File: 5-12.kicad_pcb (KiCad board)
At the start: 2 copper layers, 266.7 x 95.2 mm, 136 parts, among them SW1 SW_Push, U1 ATmega32U4-AU, Y1 16MHz

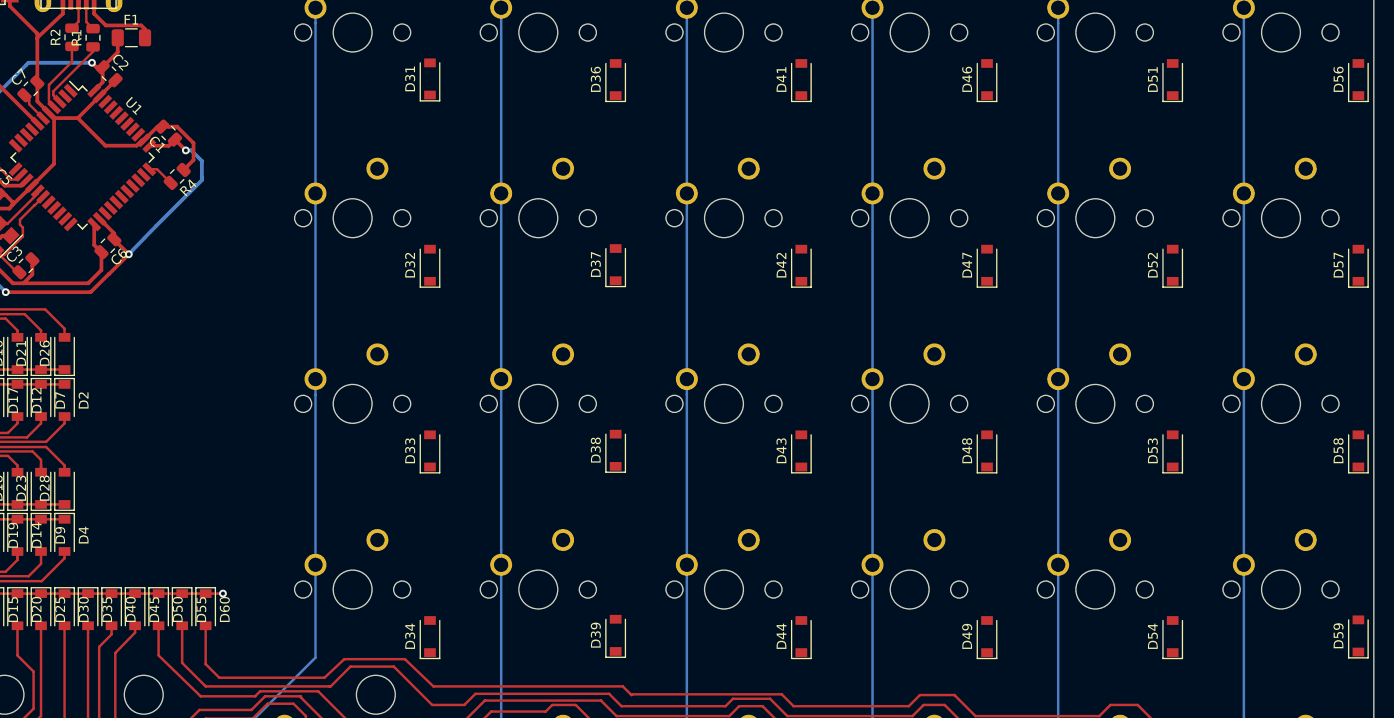
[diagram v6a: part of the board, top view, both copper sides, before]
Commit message: Positioned remainder of diode banks
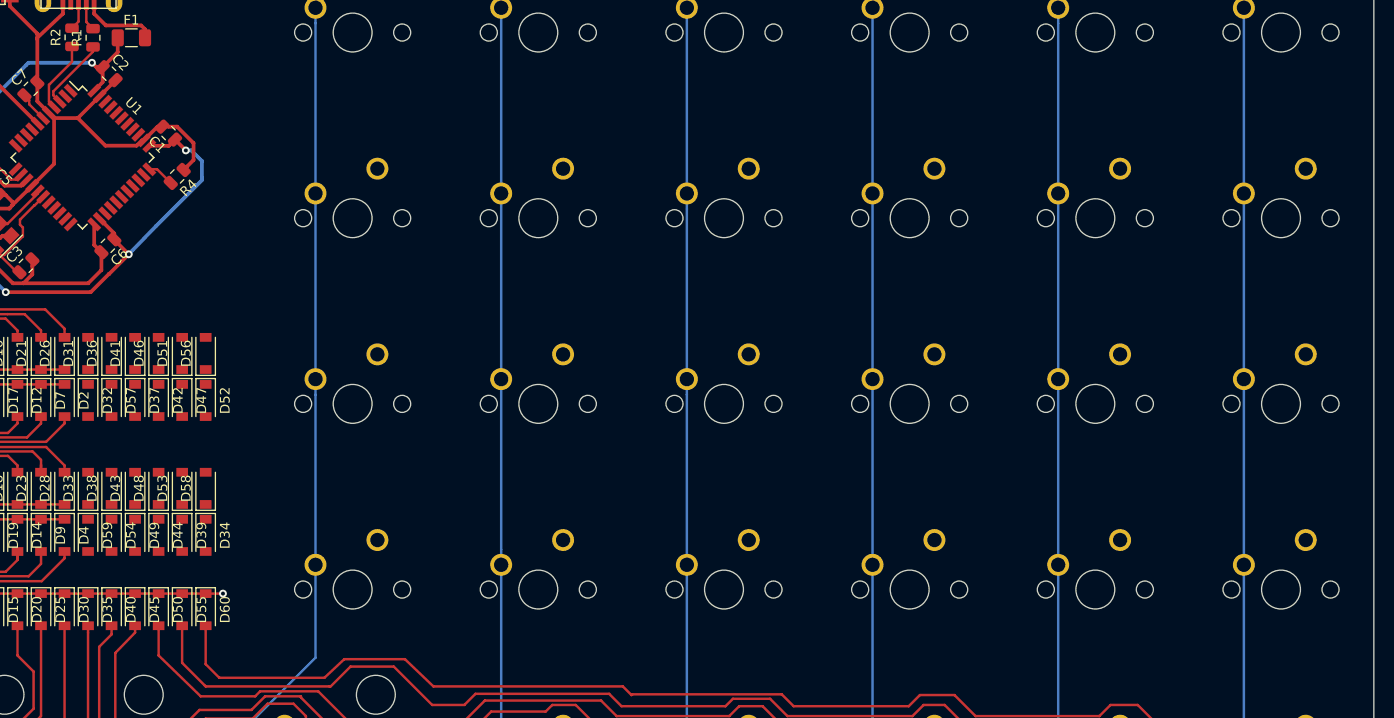
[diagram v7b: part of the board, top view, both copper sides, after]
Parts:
- moved D59 130.7 mm to (146.7, 130.2), turned to 270 degrees
- moved D57 128.7 mm to (149.1, 116.3), turned to 270 degrees
- moved D56 121.6 mm to (158.8, 111.5)
- moved D58 118.3 mm to (158.8, 125.3)
- moved D54 109.4 mm to (149.1, 130.2), turned to 270 degrees
- moved D51 105.4 mm to (156.3, 111.5)
- moved D53 101.7 mm to (156.3, 125.3)
- moved D52 100.2 mm to (158.8, 116.3), turned to 270 degrees
- moved D46 89.5 mm to (153.9, 111.5)
- moved D49 88.0 mm to (151.5, 130.2), turned to 270 degrees
- moved D48 85.1 mm to (153.9, 125.3)
- moved D47 83.7 mm to (156.3, 116.3), turned to 270 degrees
- moved D41 73.9 mm to (151.5, 111.5)
- moved D43 68.5 mm to (151.5, 125.3)
- moved D42 67.4 mm to (153.9, 116.3), turned to 270 degrees
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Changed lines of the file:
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@@
   )
   (module Diode_SMD:D_SOD-123 (layer F.Cu)
-    (at 277.01875 140.49375 90)
+    (at 146.685 130.174 270)
     (descr SOD-123)
     (tags SOD-123)
@@
       (effects (font (size 1 1) (thickness 0.15)))
     )
-    (pad 2 smd rect (at 1.65 0 90) (size 0.9 1.2) (layers F.Cu F.Paste F.Mask)
+    (pad 2 smd rect (at 1.65 0 270) (size 0.9 1.2) (layers F.Cu F.Paste F.Mask)
       (net 69 "Net-(D59-Pad2)"))
-    (pad 1 smd rect (at -1.65 0 90) (size 0.9 1.2) (layers F.Cu F.Paste F.Mask)
+    (pad 1 smd rect (at -1.65 0 270) (size 0.9 1.2) (layers F.Cu F.Paste F.Mask)
       (net 13 Row3))
     (model ${KISYS3DMOD}/Diode_SMD.3dshapes/D_SOD-123.wrl
@@
   )
   (module Diode_SMD:D_SOD-123 (layer F.Cu)
-    (at 277.01875 121.50625 90)
+    (at 158.75 125.35 90)
     (descr SOD-123)
     (tags SOD-123)
@@
   )
   (module Diode_SMD:D_SOD-123 (layer F.Cu)
-    (at 277.01875 102.45625 90)
+    (at 149.098 116.331 270)
     (descr SOD-123)
     (tags SOD-123)
@@
       (effects (font (size 1 1) (thickness 0.15)))
     )
-    (pad 2 smd rect (at 1.65 0 90) (size 0.9 1.2) (layers F.Cu F.Paste F.Mask)
+    (pad 2 smd rect (at 1.65 0 270) (size 0.9 1.2) (layers F.Cu F.Paste F.Mask)
       (net 67 "Net-(D57-Pad2)"))
-    (pad 1 smd rect (at -1.65 0 90) (size 0.9 1.2) (layers F.Cu F.Paste F.Mask)
+    (pad 1 smd rect (at -1.65 0 270) (size 0.9 1.2) (layers F.Cu F.Paste F.Mask)
       (net 9 Row1))
     (model ${KISYS3DMOD}/Diode_SMD.3dshapes/D_SOD-123.wrl
@@
   )
   (module Diode_SMD:D_SOD-123 (layer F.Cu)
-    (at 277.01875 83.40625 90)
+    (at 158.75 111.507 90)
     (descr SOD-123)
     (tags SOD-123)
@@
   )
   (module Diode_SMD:D_SOD-123 (layer F.Cu)
-    (at 257.96875 140.55625 90)
+    (at 149.098 130.174 270)
     (descr SOD-123)
     (tags SOD-123)
@@
       (effects (font (size 1 1) (thickness 0.15)))
     )
-    (pad 2 smd rect (at 1.65 0 90) (size 0.9 1.2) (layers F.Cu F.Paste F.Mask)
+    (pad 2 smd rect (at 1.65 0 270) (size 0.9 1.2) (layers F.Cu F.Paste F.Mask)
       (net 64 "Net-(D54-Pad2)"))
-    (pad 1 smd rect (at -1.65 0 90) (size 0.9 1.2) (layers F.Cu F.Paste F.Mask)
+    (pad 1 smd rect (at -1.65 0 270) (size 0.9 1.2) (layers F.Cu F.Paste F.Mask)
       (net 13 Row3))
     (model ${KISYS3DMOD}/Diode_SMD.3dshapes/D_SOD-123.wrl
@@
   )
   (module Diode_SMD:D_SOD-123 (layer F.Cu)
-    (at 257.96875 121.50625 90)
+    (at 156.337 125.35 90)
     (descr SOD-123)
     (tags SOD-123)
@@
   )
   (module Diode_SMD:D_SOD-123 (layer F.Cu)
-    (at 257.96875 102.45625 90)
+    (at 158.75 116.333 270)
     (descr SOD-123)
     (tags SOD-123)
@@
       (effects (font (size 1 1) (thickness 0.15)))
     )
-    (pad 2 smd rect (at 1.65 0 90) (size 0.9 1.2) (layers F.Cu F.Paste F.Mask)
+    (pad 2 smd rect (at 1.65 0 270) (size 0.9 1.2) (layers F.Cu F.Paste F.Mask)
       (net 62 "Net-(D52-Pad2)"))
-    (pad 1 smd rect (at -1.65 0 90) (size 0.9 1.2) (layers F.Cu F.Paste F.Mask)
+    (pad 1 smd rect (at -1.65 0 270) (size 0.9 1.2) (layers F.Cu F.Paste F.Mask)
       (net 9 Row1))
     (model ${KISYS3DMOD}/Diode_SMD.3dshapes/D_SOD-123.wrl
@@
   )
   (module Diode_SMD:D_SOD-123 (layer F.Cu)
-    (at 257.96875 83.40625 90)
+    (at 156.337 111.507 90)
     (descr SOD-123)
     (tags SOD-123)
@@
   )
   (module Diode_SMD:D_SOD-123 (layer F.Cu)
-    (at 238.91875 140.55625 90)
+    (at 151.511 130.174 270)
     (descr SOD-123)
     (tags SOD-123)
@@
       (effects (font (size 1 1) (thickness 0.15)))
     )
-    (pad 2 smd rect (at 1.65 0 90) (size 0.9 1.2) (layers F.Cu F.Paste F.Mask)
+    (pad 2 smd rect (at 1.65 0 270) (size 0.9 1.2) (layers F.Cu F.Paste F.Mask)
       (net 59 "Net-(D49-Pad2)"))
-    (pad 1 smd rect (at -1.65 0 90) (size 0.9 1.2) (layers F.Cu F.Paste F.Mask)
+    (pad 1 smd rect (at -1.65 0 270) (size 0.9 1.2) (layers F.Cu F.Paste F.Mask)
       (net 13 Row3))
     (model ${KISYS3DMOD}/Diode_SMD.3dshapes/D_SOD-123.wrl
@@
   )
   (module Diode_SMD:D_SOD-123 (layer F.Cu)
-    (at 238.91875 121.50625 90)
+    (at 153.924 125.35 90)
     (descr SOD-123)
     (tags SOD-123)
@@
   )
   (module Diode_SMD:D_SOD-123 (layer F.Cu)
-    (at 238.91875 102.45625 90)
+    (at 156.337 116.331 270)
     (descr SOD-123)
     (tags SOD-123)
@@
       (effects (font (size 1 1) (thickness 0.15)))
     )
-    (pad 2 smd rect (at 1.65 0 90) (size 0.9 1.2) (layers F.Cu F.Paste F.Mask)
+    (pad 2 smd rect (at 1.65 0 270) (size 0.9 1.2) (layers F.Cu F.Paste F.Mask)
       (net 57 "Net-(D47-Pad2)"))
-    (pad 1 smd rect (at -1.65 0 90) (size 0.9 1.2) (layers F.Cu F.Paste F.Mask)
+    (pad 1 smd rect (at -1.65 0 270) (size 0.9 1.2) (layers F.Cu F.Paste F.Mask)
       (net 9 Row1))
     (model ${KISYS3DMOD}/Diode_SMD.3dshapes/D_SOD-123.wrl
@@
   )
   (module Diode_SMD:D_SOD-123 (layer F.Cu)
-    (at 238.91875 83.40625 90)
+    (at 153.924 111.507 90)
     (descr SOD-123)
     (tags SOD-123)
@@
   )
   (module Diode_SMD:D_SOD-123 (layer F.Cu)
-    (at 219.86875 140.55625 90)
+    (at 153.924 130.174 270)
     (descr SOD-123)
     (tags SOD-123)
@@
       (effects (font (size 1 1) (thickness 0.15)))
     )
-    (pad 2 smd rect (at 1.65 0 90) (size 0.9 1.2) (layers F.Cu F.Paste F.Mask)
+    (pad 2 smd rect (at 1.65 0 270) (size 0.9 1.2) (layers F.Cu F.Paste F.Mask)
       (net 54 "Net-(D44-Pad2)"))
-    (pad 1 smd rect (at -1.65 0 90) (size 0.9 1.2) (layers F.Cu F.Paste F.Mask)
+    (pad 1 smd rect (at -1.65 0 270) (size 0.9 1.2) (layers F.Cu F.Paste F.Mask)
       (net 13 Row3))
     (model ${KISYS3DMOD}/Diode_SMD.3dshapes/D_SOD-123.wrl
@@
   )
   (module Diode_SMD:D_SOD-123 (layer F.Cu)
-    (at 219.86875 121.50625 90)
+    (at 151.511 125.35 90)
     (descr SOD-123)
     (tags SOD-123)
@@
   )
   (module Diode_SMD:D_SOD-123 (layer F.Cu)
-    (at 219.86875 102.45625 90)
+    (at 153.924 116.331 270)
     (descr SOD-123)
     (tags SOD-123)
@@
       (effects (font (size 1 1) (thickness 0.15)))
     )
-    (pad 2 smd rect (at 1.65 0 90) (size 0.9 1.2) (layers F.Cu F.Paste F.Mask)
+    (pad 2 smd rect (at 1.65 0 270) (size 0.9 1.2) (layers F.Cu F.Paste F.Mask)
       (net 52 "Net-(D42-Pad2)"))
-    (pad 1 smd rect (at -1.65 0 90) (size 0.9 1.2) (layers F.Cu F.Paste F.Mask)
+    (pad 1 smd rect (at -1.65 0 270) (size 0.9 1.2) (layers F.Cu F.Paste F.Mask)
       (net 9 Row1))
     (model ${KISYS3DMOD}/Diode_SMD.3dshapes/D_SOD-123.wrl
@@
   )
   (module Diode_SMD:D_SOD-123 (layer F.Cu)
-    (at 219.86875 83.40625 90)
+    (at 151.511 111.507 90)
     (descr SOD-123)
     (tags SOD-123)
@@
   )
   (module Diode_SMD:D_SOD-123 (layer F.Cu)
-    (at 200.81875 140.43125 90)
+    (at 156.337 130.174 270)
     (descr SOD-123)
     (tags SOD-123)
@@
       (effects (font (size 1 1) (thickness 0.15)))
     )
-    (pad 2 smd rect (at 1.65 0 90) (size 0.9 1.2) (layers F.Cu F.Paste F.Mask)
+    (pad 2 smd rect (at 1.65 0 270) (size 0.9 1.2) (layers F.Cu F.Paste F.Mask)
       (net 49 "Net-(D39-Pad2)"))
-    (pad 1 smd rect (at -1.65 0 90) (size 0.9 1.2) (layers F.Cu F.Paste F.Mask)
+    (pad 1 smd rect (at -1.65 0 270) (size 0.9 1.2) (layers F.Cu F.Paste F.Mask)
       (net 13 Row3))
     (model ${KISYS3DMOD}/Diode_SMD.3dshapes/D_SOD-123.wrl
@@
   )
   (module Diode_SMD:D_SOD-123 (layer F.Cu)
-    (at 200.81875 121.44375 90)
+    (at 149.098 125.35 90)
     (descr SOD-123)
     (tags SOD-123)
@@
   )
   (module Diode_SMD:D_SOD-123 (layer F.Cu)
-    (at 200.81875 102.39375 90)
+    (at 151.511 116.331 270)
     (descr SOD-123)
     (tags SOD-123)
@@
       (effects (font (size 1 1) (thickness 0.15)))
     )
-    (pad 2 smd rect (at 1.65 0 90) (size 0.9 1.2) (layers F.Cu F.Paste F.Mask)
+    (pad 2 smd rect (at 1.65 0 270) (size 0.9 1.2) (layers F.Cu F.Paste F.Mask)
       (net 47 "Net-(D37-Pad2)"))
-    (pad 1 smd rect (at -1.65 0 90) (size 0.9 1.2) (layers F.Cu F.Paste F.Mask)
+    (pad 1 smd rect (at -1.65 0 270) (size 0.9 1.2) (layers F.Cu F.Paste F.Mask)
       (net 9 Row1))
     (model ${KISYS3DMOD}/Diode_SMD.3dshapes/D_SOD-123.wrl
@@
   )
   (module Diode_SMD:D_SOD-123 (layer F.Cu)
-    (at 200.81875 83.40625 90)
+    (at 149.098 111.506 90)
     (descr SOD-123)
     (tags SOD-123)
@@
   )
   (module Diode_SMD:D_SOD-123 (layer F.Cu)
-    (at 181.76875 140.55625 90)
+    (at 158.75 130.174 270)
     (descr SOD-123)
     (tags SOD-123)
@@
       (effects (font (size 1 1) (thickness 0.15)))
     )
-    (pad 2 smd rect (at 1.65 0 90) (size 0.9 1.2) (layers F.Cu F.Paste F.Mask)
+    (pad 2 smd rect (at 1.65 0 270) (size 0.9 1.2) (layers F.Cu F.Paste F.Mask)
       (net 44 "Net-(D34-Pad2)"))
-    (pad 1 smd rect (at -1.65 0 90) (size 0.9 1.2) (layers F.Cu F.Paste F.Mask)
+    (pad 1 smd rect (at -1.65 0 270) (size 0.9 1.2) (layers F.Cu F.Paste F.Mask)
       (net 13 Row3))
     (model ${KISYS3DMOD}/Diode_SMD.3dshapes/D_SOD-123.wrl
@@
   )
   (module Diode_SMD:D_SOD-123 (layer F.Cu)
-    (at 181.76875 121.50625 90)
+    (at 146.685 125.35 90)
     (descr SOD-123)
     (tags SOD-123)
@@
   )
   (module Diode_SMD:D_SOD-123 (layer F.Cu)
-    (at 181.76875 102.45625 90)
+    (at 146.685 116.331 270)
     (descr SOD-123)
     (tags SOD-123)
@@
       (effects (font (size 1 1) (thickness 0.15)))
     )
-    (pad 2 smd rect (at 1.65 0 90) (size 0.9 1.2) (layers F.Cu F.Paste F.Mask)
+    (pad 2 smd rect (at 1.65 0 270) (size 0.9 1.2) (layers F.Cu F.Paste F.Mask)
       (net 42 "Net-(D32-Pad2)"))
-    (pad 1 smd rect (at -1.65 0 90) (size 0.9 1.2) (layers F.Cu F.Paste F.Mask)
+    (pad 1 smd rect (at -1.65 0 270) (size 0.9 1.2) (layers F.Cu F.Paste F.Mask)
       (net 9 Row1))
     (model ${KISYS3DMOD}/Diode_SMD.3dshapes/D_SOD-123.wrl
@@
   )
   (module Diode_SMD:D_SOD-123 (layer F.Cu)
-    (at 181.76875 83.34375 90)
-    (descr SOD-123)
-    (tags SOD-123)
+    (at 146.685 111.507 90)
+    (descr SOD-123)
+    (tags SOD-123)

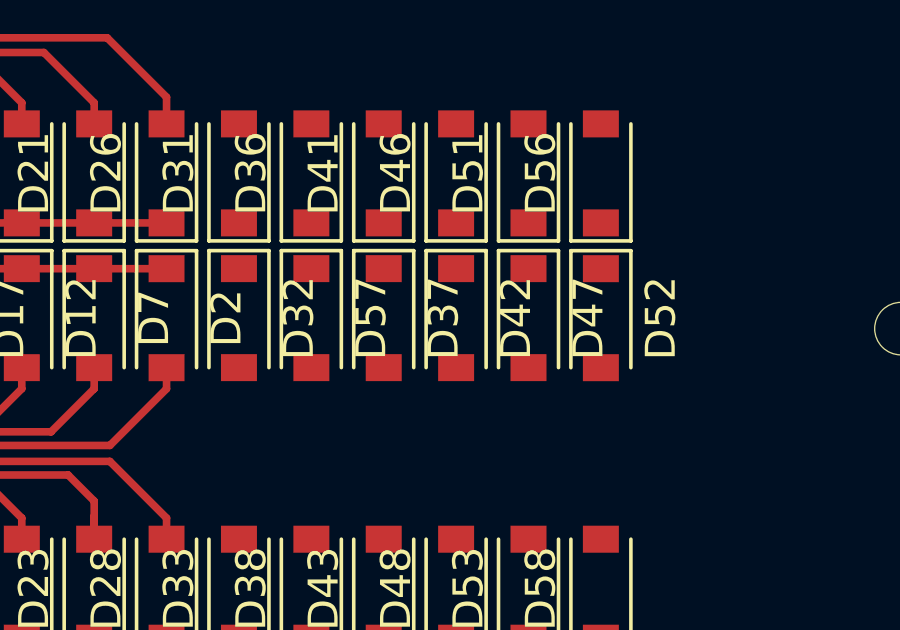
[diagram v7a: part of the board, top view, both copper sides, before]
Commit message: Reordered a right row diode bank for proper arrangement
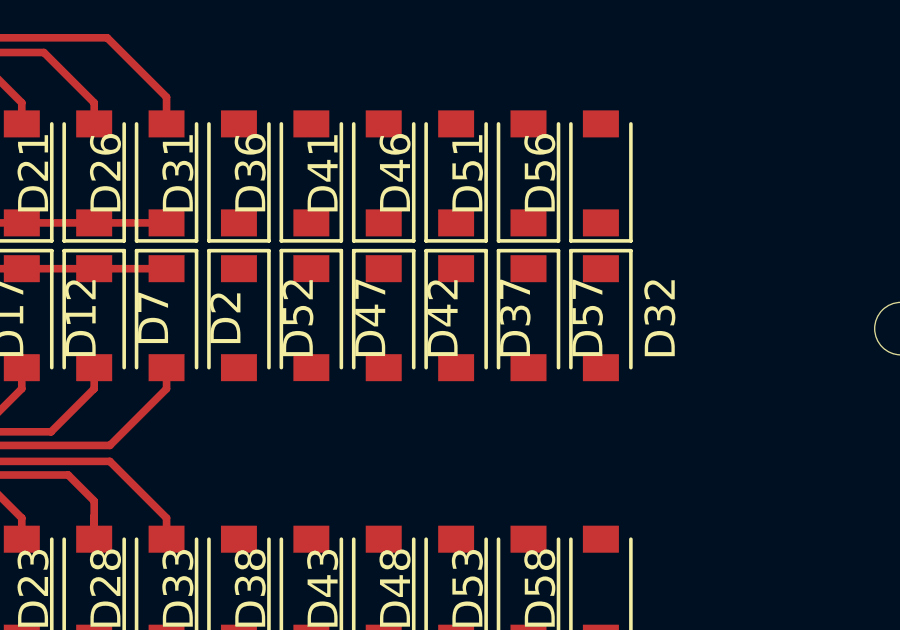
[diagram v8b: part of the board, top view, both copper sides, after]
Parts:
- moved D32 12.1 mm to (158.8, 116.3)
- moved D52 12.1 mm to (146.7, 116.3)
- moved D57 7.24 mm to (156.3, 116.3)
- moved D47 7.24 mm to (149.1, 116.3)
- moved D37 2.41 mm to (153.9, 116.3)
- moved D42 2.41 mm to (151.5, 116.3)
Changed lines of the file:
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@@
   )
   (module Diode_SMD:D_SOD-123 (layer F.Cu)
-    (at 149.098 116.331 270)
+    (at 156.337 116.333 270)
     (descr SOD-123)
     (tags SOD-123)
@@
   )
   (module Diode_SMD:D_SOD-123 (layer F.Cu)
-    (at 158.75 116.333 270)
+    (at 146.685 116.333 270)
     (descr SOD-123)
     (tags SOD-123)
@@
   )
   (module Diode_SMD:D_SOD-123 (layer F.Cu)
-    (at 156.337 116.331 270)
+    (at 149.098 116.331 270)
     (descr SOD-123)
     (tags SOD-123)
@@
   )
   (module Diode_SMD:D_SOD-123 (layer F.Cu)
-    (at 153.924 116.331 270)
+    (at 151.511 116.333 270)
     (descr SOD-123)
     (tags SOD-123)
@@
   )
   (module Diode_SMD:D_SOD-123 (layer F.Cu)
-    (at 151.511 116.331 270)
+    (at 153.924 116.333 270)
     (descr SOD-123)
     (tags SOD-123)
@@
   )
   (module Diode_SMD:D_SOD-123 (layer F.Cu)
-    (at 146.685 116.331 270)
-    (descr SOD-123)
-    (tags SOD-123)
+    (at 158.75 116.333 270)
+    (descr SOD-123)
+    (tags SOD-123)
